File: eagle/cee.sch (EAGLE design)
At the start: 48 parts, among them IC1 IC1, J1 SOLDERJUMPERNC2

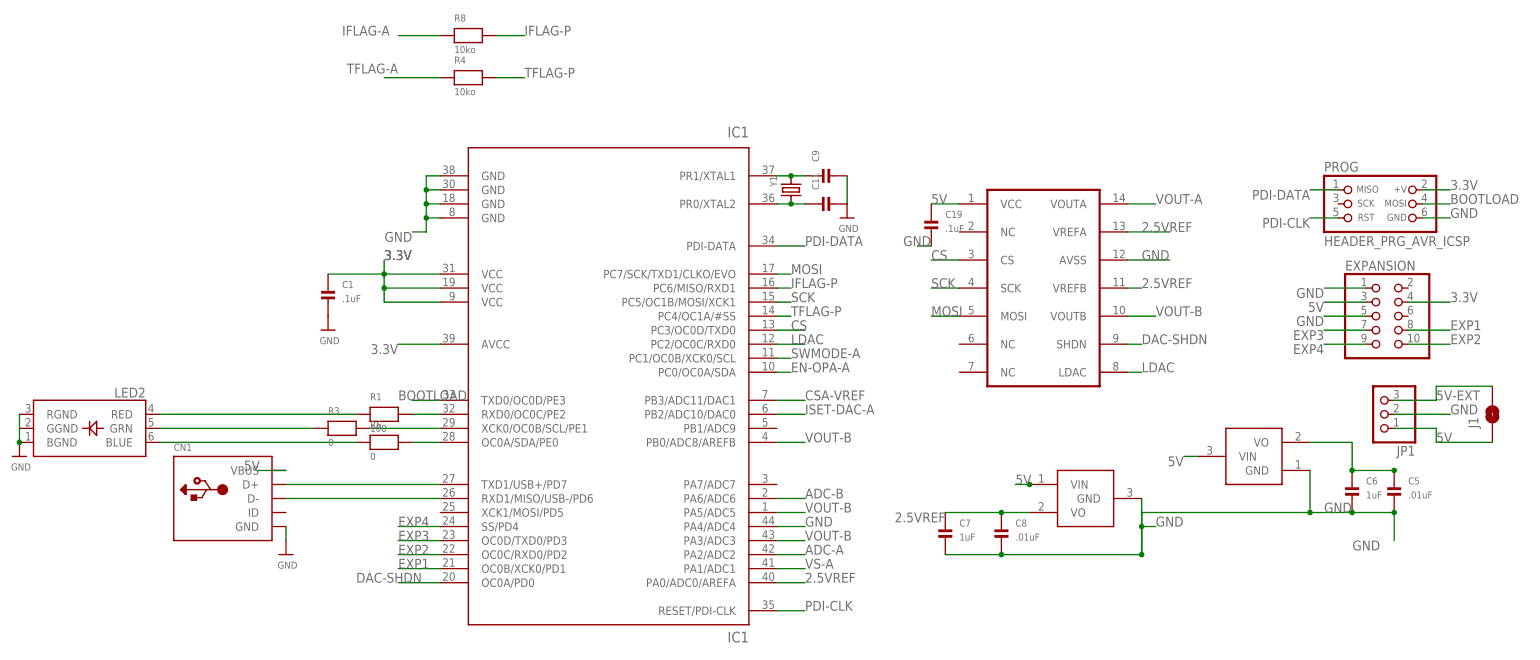
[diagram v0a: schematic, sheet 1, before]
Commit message: Break out another GPIO
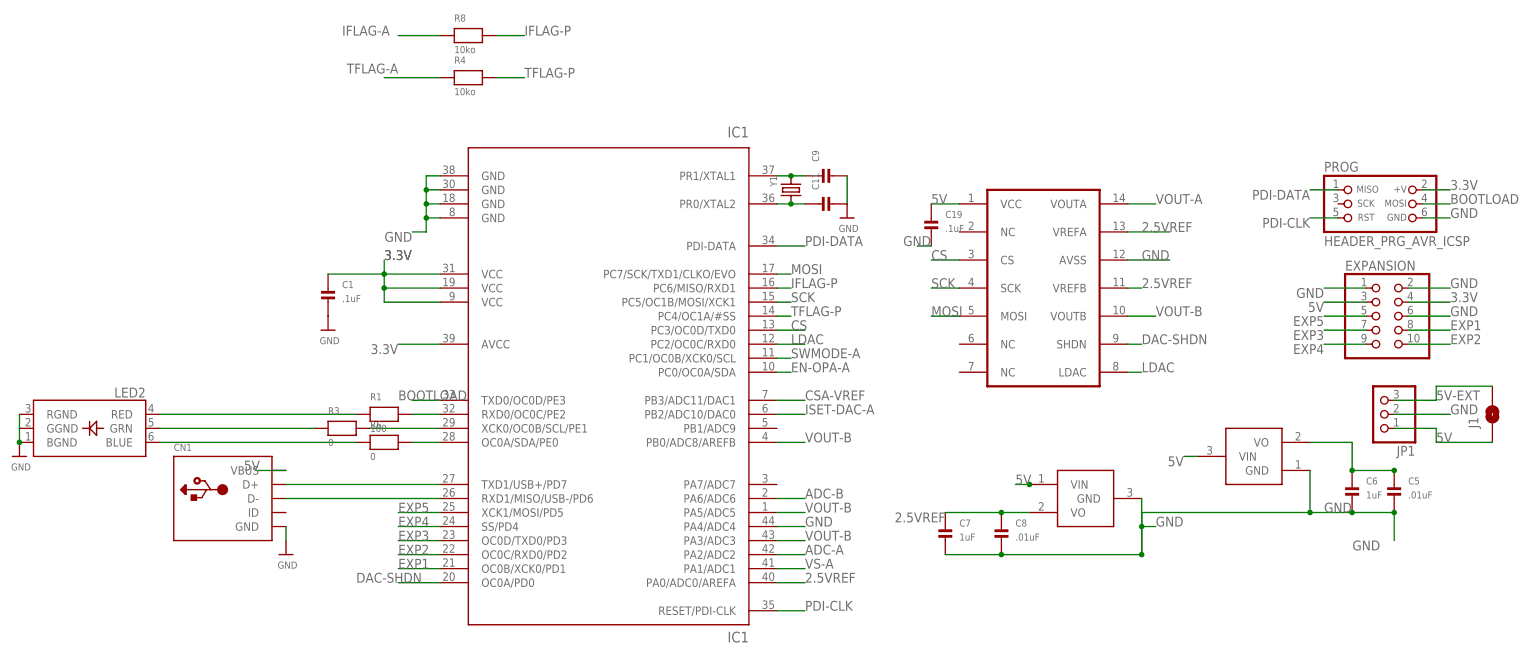
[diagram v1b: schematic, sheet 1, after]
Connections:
- new net EXP5: EXPANSION.5, IC1.XCK1/MOSI/PD5
- net GND: now also EXPANSION.2, EXPANSION.6; no longer EXPANSION.5
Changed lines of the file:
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@@
-</segment>
-<segment>
-<wire x1="203.2" y1="53.34" x2="195.58" y2="53.34" width="0" layer="91"/>
-<label x="195.58" y="53.34" size="1.778" layer="95" rot="R180"/>
-<pinref part="EXPANSION" gate="A" pin="5"/>
 </segment>
 <segment>
@@
 <pinref part="U$7" gate="G$1" pin="GND"/>
 <junction x="-40.64" y="30.48"/>
+</segment>
+<segment>
+<pinref part="EXPANSION" gate="A" pin="2"/>
+<wire x1="210.82" y1="58.42" x2="218.44" y2="58.42" width="0.1524" layer="91"/>
+<label x="218.44" y="58.42" size="1.778" layer="95"/>
+</segment>
+<segment>
+<pinref part="EXPANSION" gate="A" pin="6"/>
+<wire x1="210.82" y1="53.34" x2="218.44" y2="53.34" width="0.1524" layer="91"/>
+<label x="218.44" y="53.34" size="1.778" layer="95"/>
 </segment>
 </net>
@@
 </segment>
 </net>
+<net name="EXP5" class="0">
+<segment>
+<pinref part="IC1" gate="G$1" pin="XCK1/MOSI/PD5"/>
+<wire x1="35.56" y1="17.78" x2="27.94" y2="17.78" width="0.1524" layer="91"/>
+<label x="27.94" y="17.78" size="1.778" layer="95"/>
+</segment>
+<segment>
+<pinref part="EXPANSION" gate="A" pin="5"/>
+<wire x1="203.2" y1="53.34" x2="195.58" y2="53.34" width="0.1524" layer="91"/>
+<label x="195.58" y="53.34" size="1.778" layer="95" rot="R180"/>
+</segment>
+</net>

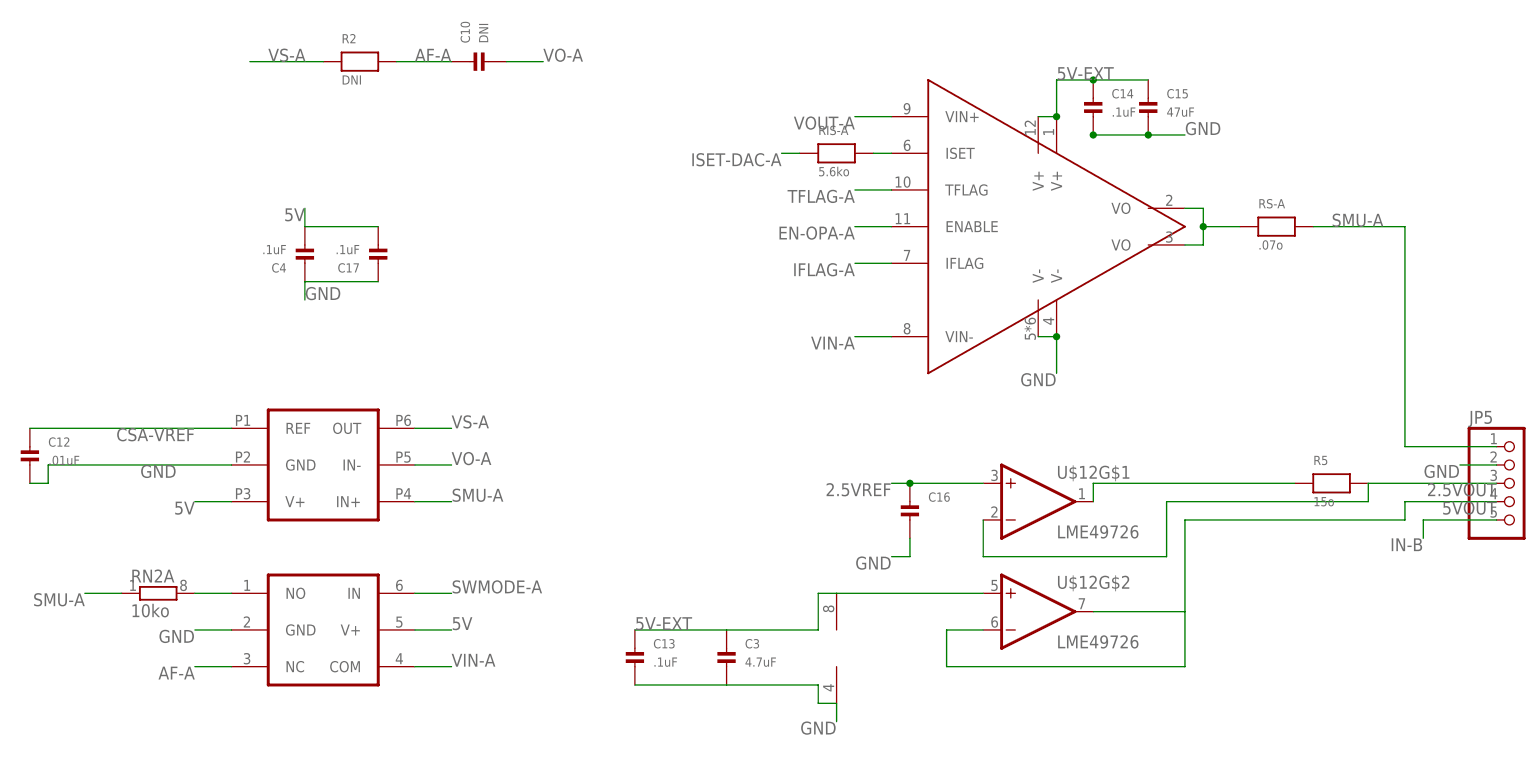
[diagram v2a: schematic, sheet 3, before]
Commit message: significantly revised schematic including feedback compensation loooooops and mcp6n11
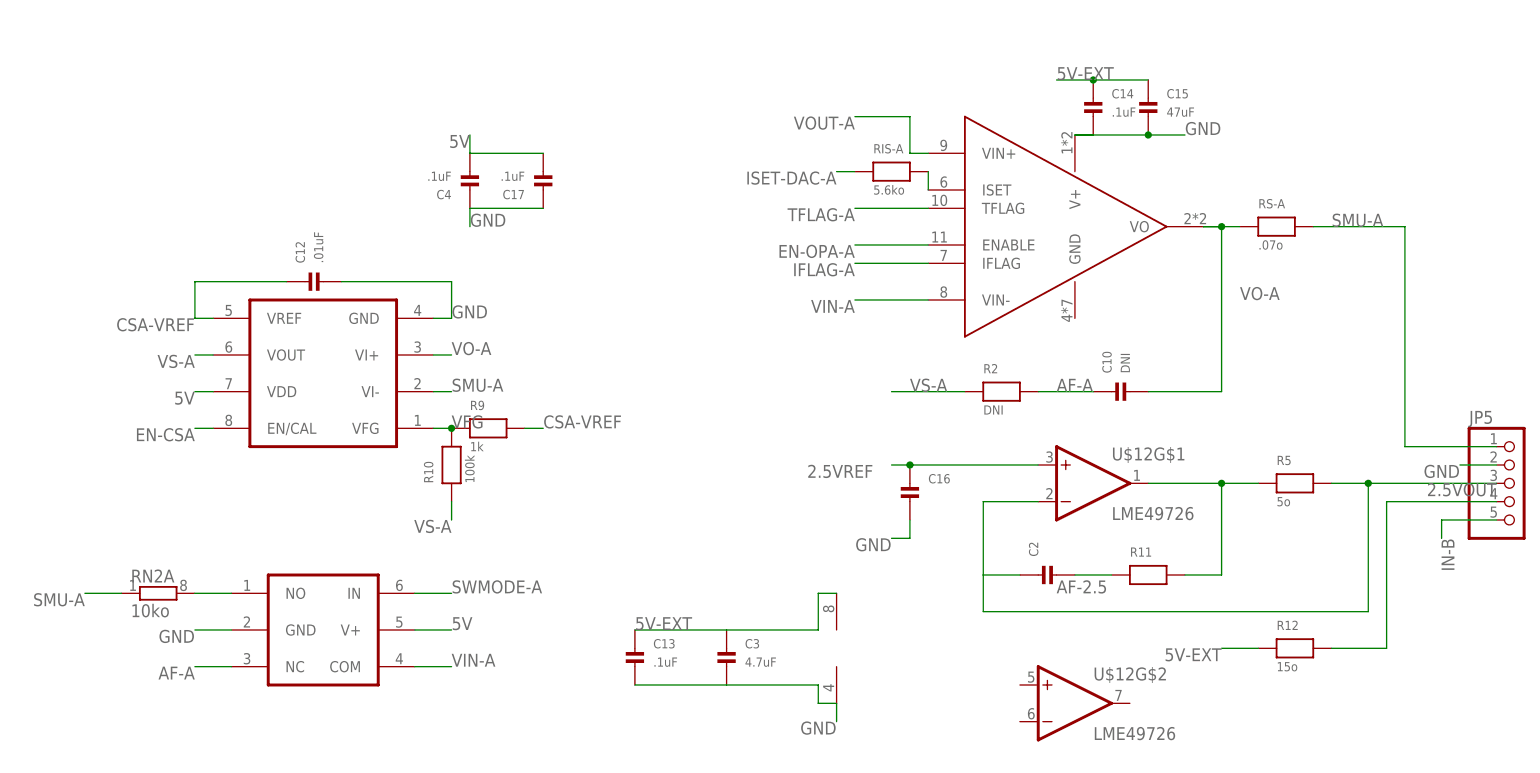
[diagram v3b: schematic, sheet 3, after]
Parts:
- removed CS-A: INA213, nonolith:INA213
- added C2: (no value), nonolith:CAP_CERAMIC0603
- added R10: 100k, nonolith:RESISTOR0603
- added R11: (no value), nonolith:RESISTOR0603
- added R12: 15o, nonolith:RESISTOR1206
- added R9: 1k, nonolith:RESISTOR0603
- added U$13: MCP6N11, nonolith:MCP6N11
- 3.3VREG: value VREG -> VREGMCP1700; device nonolith:VREG -> nonolith:VREGMCP1700
- R5: value 15o -> 5o
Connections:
- removed net 5VOUT: JP5.4, U$12G$2.-IN, U$12G$2.OUT
- new net AF-2.5: C2.P$2, R11.1
- new net EN-CSA: U$13.EN/CAL
- new net N$14: JP5.4, R12.2
- new net VFG: R10.2, R9.1, U$13.VFG
- net 2.5VFDBK: now also R11.2
- net 2.5VOUT: now also C2.P$1
- net 5V: now also U$13.VDD; no longer CS-A.V+
- net 5V-EXT: now also R12.1; no longer OPA-A.V+@1, OPA-A.V+@12, U$12G$2.+IN
- net CSA-VREF: now also R9.2, U$13.VREF; no longer CS-A.REF
- net GND: now also OPA-A.V+, U$13.GND; no longer CS-A.GND, OPA-A.V-@4, OPA-A.V-@5
- net SMU-A: now also U$13.VI-; no longer CS-A.IN+
- net VO-A: now also OPA-A.VO, U$13.VI+; no longer CS-A.IN-, OPA-A.VO@2, OPA-A.VO@3
- net VS-A: now also R10.1, U$13.VOUT; no longer CS-A.OUT
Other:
- moved on the sheet: C10, C12, C16, C17, C4, R2, R5, RIS-A, U$12G$1, U$12G$2

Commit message: move SIMV minor loop from '567 to around CSA for functionality clarification
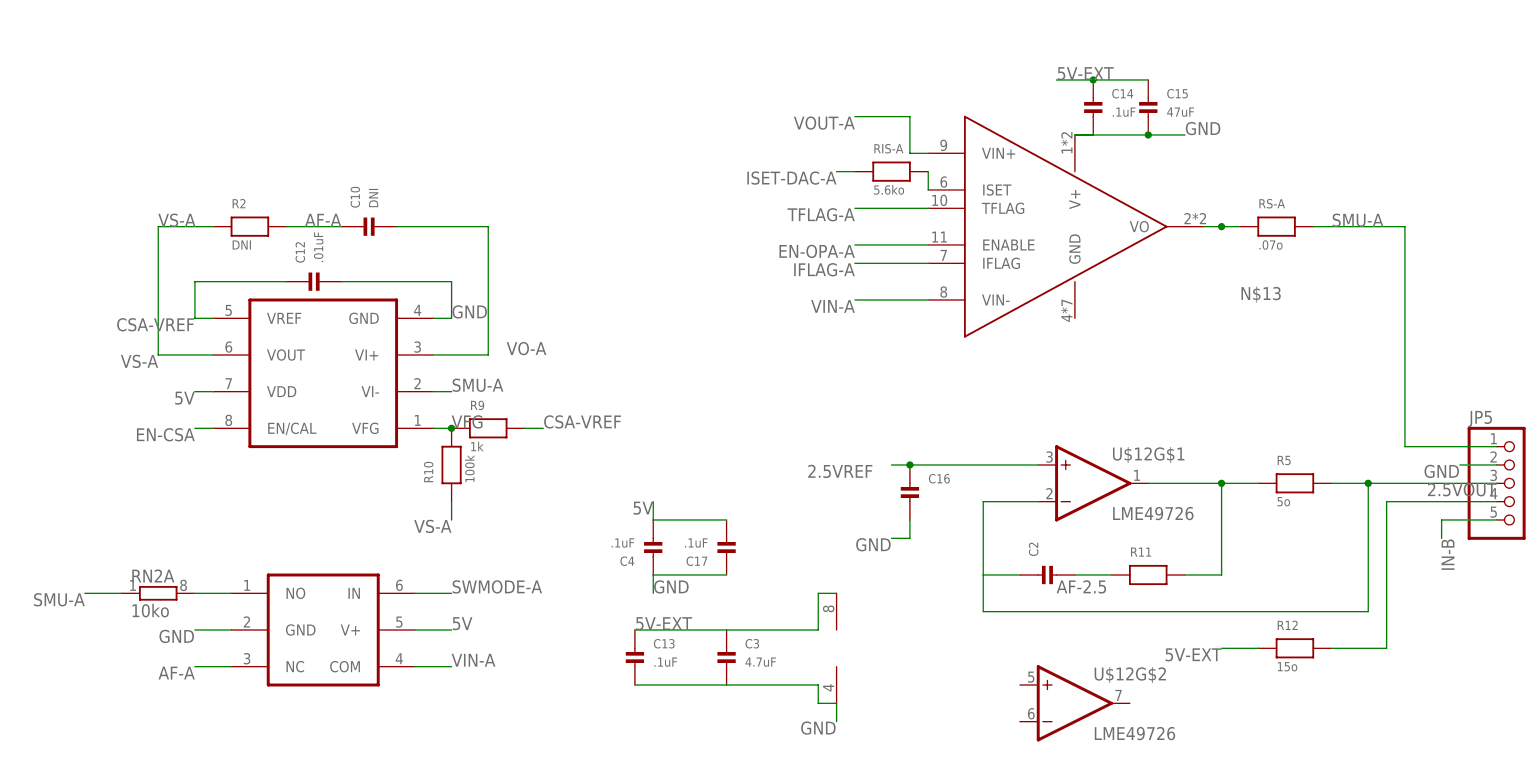
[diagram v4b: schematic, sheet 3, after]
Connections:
- new net N$13: OPA-A.VO, RS-A.1
- net VO-A: no longer OPA-A.VO, RS-A.1
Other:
- moved on the sheet: C10, C17, C4, R2
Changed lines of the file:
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@@
 <instance part="C14" gate="G$1" x="142.24" y="111.76"/>
 <instance part="C15" gate="G$1" x="149.86" y="111.76"/>
-<instance part="C4" gate="G$1" x="55.88" y="104.14" rot="R180"/>
-<instance part="R2" gate="G$1" x="129.54" y="73.66"/>
-<instance part="C10" gate="G$1" x="147.32" y="73.66" rot="R90"/>
+<instance part="C4" gate="G$1" x="81.28" y="53.34" rot="R180"/>
+<instance part="R2" gate="G$1" x="25.4" y="96.52"/>
+<instance part="C10" gate="G$1" x="43.18" y="96.52" rot="R90"/>
 <instance part="RN2" gate="A" x="12.7" y="45.72"/>
 <instance part="JP5" gate="A" x="200.66" y="60.96"/>
@@
 <instance part="C13" gate="G$1" x="78.74" y="35.56"/>
 <instance part="C16" gate="G$1" x="116.84" y="58.42"/>
-<instance part="C17" gate="G$1" x="66.04" y="104.14" rot="R180"/>
+<instance part="C17" gate="G$1" x="91.44" y="53.34" rot="R180"/>
 <instance part="U$13" gate="G$1" x="35.56" y="76.2" rot="R180"/>
 <instance part="R9" gate="G$1" x="58.42" y="68.58"/>
@@
 </segment>
 <segment>
-<wire x1="55.88" y1="109.22" x2="55.88" y2="106.68" width="0.254" layer="91"/>
-<label x="55.88" y="109.22" size="1.778" layer="95" rot="R180"/>
+<wire x1="81.28" y1="58.42" x2="81.28" y2="55.88" width="0.254" layer="91"/>
+<label x="81.28" y="58.42" size="1.778" layer="95" rot="R180"/>
 <pinref part="C4" gate="G$1" pin="P$2"/>
 <pinref part="C17" gate="G$1" pin="P$2"/>
-<wire x1="55.88" y1="106.68" x2="66.04" y2="106.68" width="0.254" layer="91"/>
+<wire x1="81.28" y1="55.88" x2="91.44" y2="55.88" width="0.254" layer="91"/>
 </segment>
 <segment>
@@
 <segment>
 <pinref part="C4" gate="G$1" pin="P$1"/>
-<wire x1="55.88" y1="99.06" x2="55.88" y2="96.52" width="0.254" layer="91"/>
-<label x="55.88" y="96.52" size="1.778" layer="95"/>
+<wire x1="81.28" y1="48.26" x2="81.28" y2="45.72" width="0.254" layer="91"/>
+<label x="81.28" y="45.72" size="1.778" layer="95"/>
 <pinref part="C17" gate="G$1" pin="P$1"/>
-<wire x1="66.04" y1="99.06" x2="55.88" y2="99.06" width="0.254" layer="91"/>
+<wire x1="91.44" y1="48.26" x2="81.28" y2="48.26" width="0.254" layer="91"/>
 </segment>
 <segment>
@@
 <net name="VO-A" class="0">
 <segment>
-<wire x1="149.86" y1="73.66" x2="160.02" y2="73.66" width="0.254" layer="91"/>
 <pinref part="C10" gate="G$1" pin="P$2"/>
-<pinref part="RS-A" gate="G$1" pin="1"/>
-<wire x1="157.48" y1="96.52" x2="160.02" y2="96.52" width="0.254" layer="91"/>
-<wire x1="160.02" y1="96.52" x2="162.56" y2="96.52" width="0.254" layer="91"/>
-<wire x1="160.02" y1="73.66" x2="160.02" y2="96.52" width="0.254" layer="91"/>
-<wire x1="160.02" y1="96.52" x2="157.48" y2="96.52" width="0.254" layer="91"/>
-<pinref part="OPA-A" gate="G$1" pin="VO"/>
-<junction x="160.02" y="96.52"/>
-<label x="162.56" y="86.36" size="1.778" layer="95"/>
-</segment>
-<segment>
+<wire x1="45.72" y1="96.52" x2="58.42" y2="96.52" width="0.254" layer="91"/>
+<wire x1="58.42" y1="96.52" x2="58.42" y2="78.74" width="0.254" layer="91"/>
 <pinref part="U$13" gate="G$1" pin="VI+"/>
-<wire x1="50.8" y1="78.74" x2="53.34" y2="78.74" width="0.254" layer="91"/>
-<label x="53.34" y="78.74" size="1.778" layer="95"/>
+<label x="60.96" y="78.74" size="1.778" layer="95"/>
+<wire x1="58.42" y1="78.74" x2="50.8" y2="78.74" width="0.254" layer="91"/>
 </segment>
 </net>
@@
 <net name="VS-A" class="0">
 <segment>
-<wire x1="114.3" y1="73.66" x2="124.46" y2="73.66" width="0.254" layer="91"/>
-<label x="116.84" y="73.66" size="1.778" layer="95"/>
+<label x="12.7" y="96.52" size="1.778" layer="95"/>
 <pinref part="R2" gate="G$1" pin="1"/>
-</segment>
-<segment>
+<wire x1="20.32" y1="96.52" x2="12.7" y2="96.52" width="0.254" layer="91"/>
+<wire x1="12.7" y1="96.52" x2="12.7" y2="78.74" width="0.254" layer="91"/>
 <pinref part="U$13" gate="G$1" pin="VOUT"/>
-<wire x1="20.32" y1="78.74" x2="17.78" y2="78.74" width="0.254" layer="91"/>
-<label x="17.78" y="78.74" size="1.778" layer="95" rot="R180"/>
+<label x="12.7" y="78.74" size="1.778" layer="95" rot="R180"/>
+<wire x1="12.7" y1="78.74" x2="20.32" y2="78.74" width="0.254" layer="91"/>
 </segment>
 <segment>
@@
 <net name="AF-A" class="0">
 <segment>
-<wire x1="134.62" y1="73.66" x2="142.24" y2="73.66" width="0.254" layer="91"/>
-<label x="137.16" y="73.66" size="1.778" layer="95"/>
+<wire x1="30.48" y1="96.52" x2="38.1" y2="96.52" width="0.254" layer="91"/>
+<label x="33.02" y="96.52" size="1.778" layer="95"/>
 <pinref part="R2" gate="G$1" pin="2"/>
 <pinref part="C10" gate="G$1" pin="P$1"/>
@@
 </segment>
 </net>
+<net name="N$13" class="0">
+<segment>
+<pinref part="RS-A" gate="G$1" pin="1"/>
+<wire x1="160.02" y1="96.52" x2="162.56" y2="96.52" width="0.254" layer="91"/>
+<junction x="160.02" y="96.52"/>
+<wire x1="160.02" y1="96.52" x2="157.48" y2="96.52" width="0.254" layer="91"/>
+<pinref part="OPA-A" gate="G$1" pin="VO"/>
+<label x="162.56" y="86.36" size="1.778" layer="95"/>
+</segment>
+</net>

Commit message: routed, needs some cleanup
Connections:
- removed net N$13: OPA-A.VO, RS-A.1
- net GND: now also OPA-A.GND
- net VO-A: now also OPA-A.VO, RS-A.1
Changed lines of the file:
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@@
 <label x="53.34" y="83.82" size="1.778" layer="95"/>
+</segment>
+<segment>
+<pinref part="OPA-A" gate="G$1" pin="GND"/>
+<wire x1="139.7" y1="83.82" x2="139.7" y2="81.28" width="0.254" layer="91"/>
 </segment>
 </net>
@@
 <label x="60.96" y="78.74" size="1.778" layer="95"/>
 <wire x1="58.42" y1="78.74" x2="50.8" y2="78.74" width="0.254" layer="91"/>
+</segment>
+<segment>
+<pinref part="OPA-A" gate="G$1" pin="VO"/>
+<pinref part="RS-A" gate="G$1" pin="1"/>
+<wire x1="162.56" y1="96.52" x2="157.48" y2="96.52" width="0.254" layer="91"/>
+<wire x1="157.48" y1="96.52" x2="157.48" y2="93.98" width="0.254" layer="91"/>
 </segment>
 </net>
@@
 </segment>
 </net>
-<net name="N$13" class="0">
-<segment>
-<pinref part="RS-A" gate="G$1" pin="1"/>
-<wire x1="160.02" y1="96.52" x2="162.56" y2="96.52" width="0.254" layer="91"/>
-<junction x="160.02" y="96.52"/>
-<wire x1="160.02" y1="96.52" x2="157.48" y2="96.52" width="0.254" layer="91"/>
-<pinref part="OPA-A" gate="G$1" pin="VO"/>
-<label x="162.56" y="86.36" size="1.778" layer="95"/>
-</segment>
-</net>
